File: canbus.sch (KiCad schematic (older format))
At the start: 12 parts

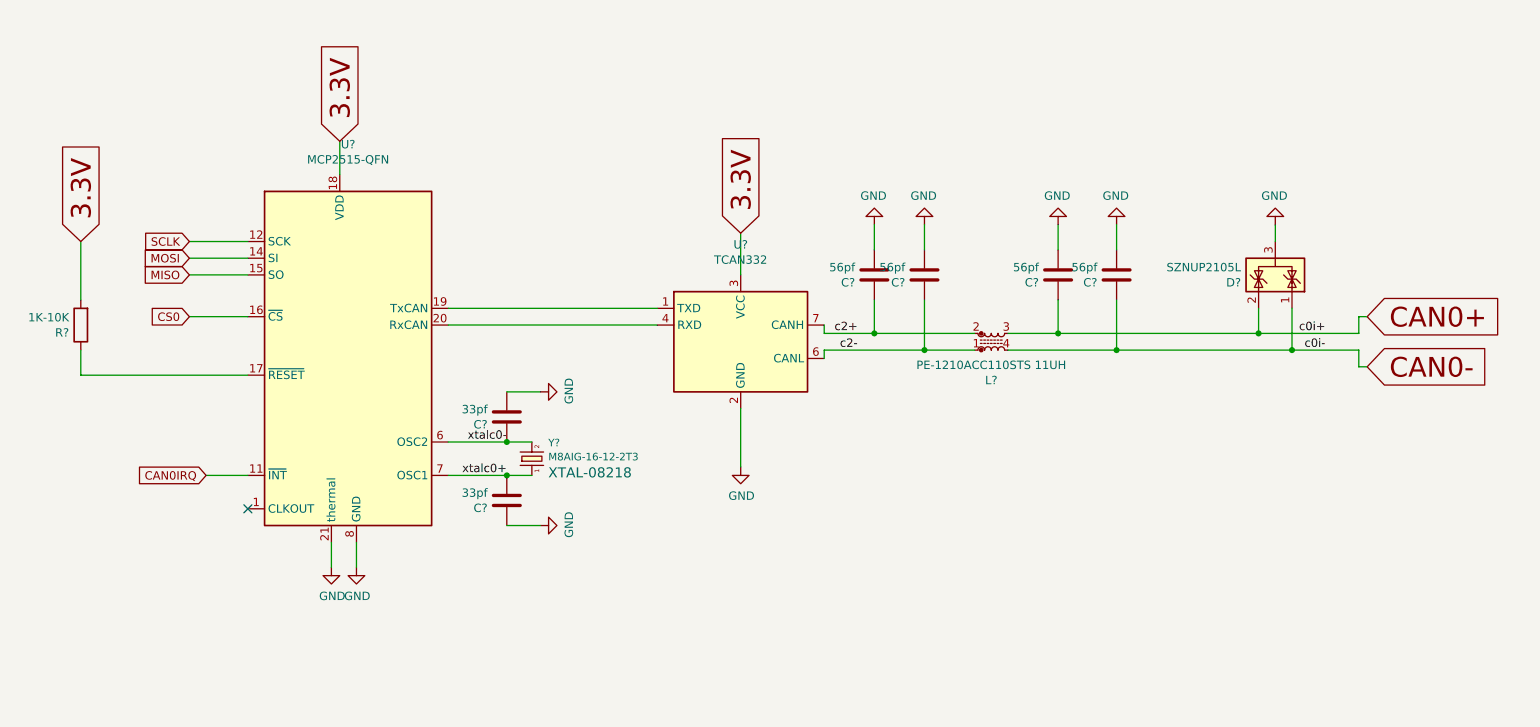
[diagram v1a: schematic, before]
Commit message: Esp32 & Canbus Sch. edited.
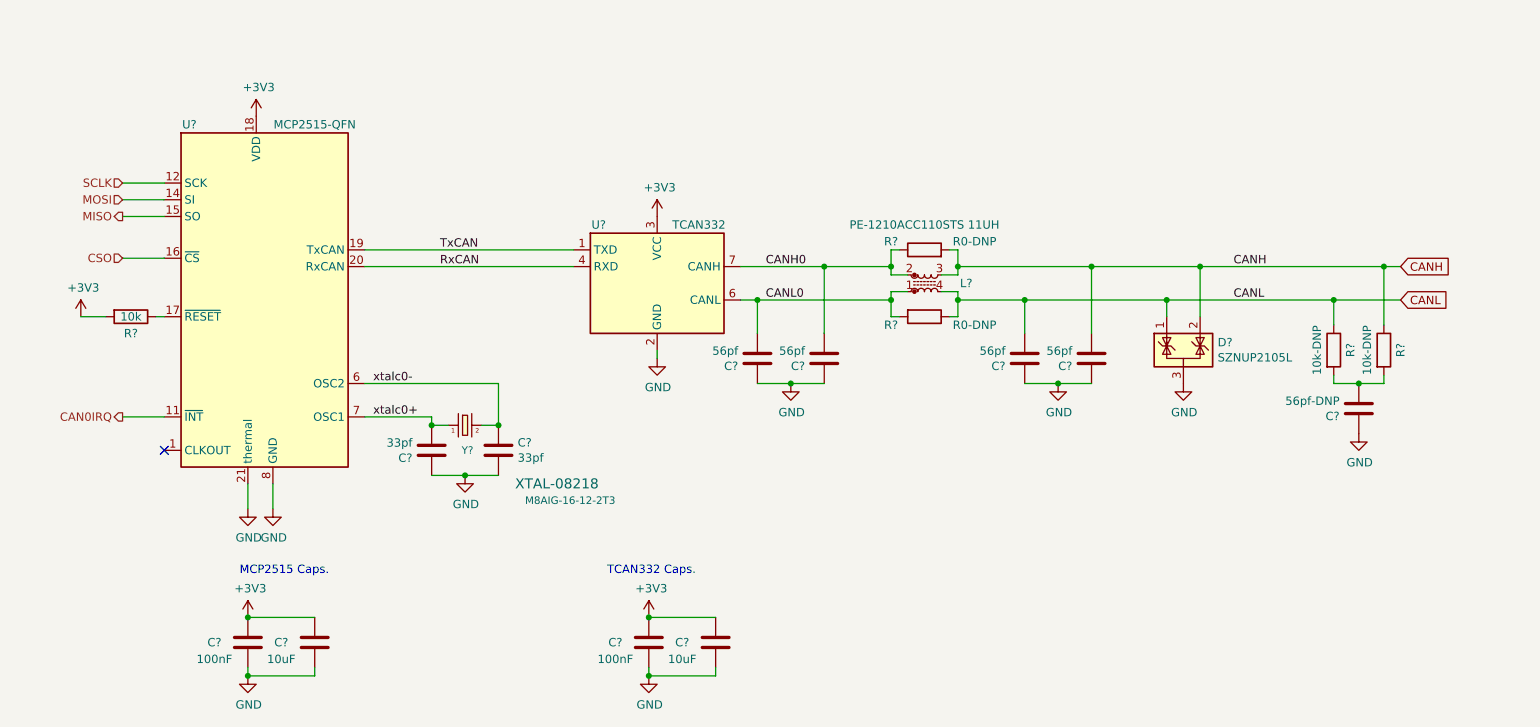
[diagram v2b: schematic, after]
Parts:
- removed C? (x2): 56pf, Capacitor_SMD:C_0603_1608Metric, symbol Device:C
- removed R?: 1K-10K, Resistor_SMD:R_0603_1608Metric, symbol Device:R
- added C? (x2): 10uF, Capacitor_SMD:C_0603_1608Metric, symbol Device:C
- added C? (x2): 100nF, Capacitor_SMD:C_0603_1608Metric, symbol Device:C
- added C? (x2): 56pf, Capacitor_SMD:C_0603_1608Metric, symbol Device:C
- added C?: 56pf-DNP, Capacitor_SMD:C_0603_1608Metric, symbol Device:C
- added R?: 10k, Resistors:0603, symbol Device:R
- added R? (x2): 10k-DNP, Resistors:0603, symbol Device:R
- added R? (x2): R0-DNP, Resistors:0603, symbol Device:R
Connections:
- net GND: now also C?.1, C?.1, C?.1, C?.1, C?.1, C?.2, C?.2, C?.2, C?.2; no longer C?.2, C?.2
- net at U?.17 (~RESET): now also R?.1
- net TxCAN: now reaches U?.1 (TXD), U?.19 (TxCAN)
- net RxCAN: now reaches U?.20 (RxCAN), U?.4 (RXD)
- net 3.3V renamed +3V3
- net +3V3: now also C?.1, C?.1, C?.1, C?.1, R?.2
- net CAN0+ renamed CANH
- net CANH: now also C?.2, R?.1, R?.2
- net CAN0- renamed CANL
- net CANL: now also C?.2, R?.1, R?.1
- net CS0 renamed CSO
- net c2+ renamed CANH0
- net CANH0: now also C?.2, R?.1; no longer C?.1
- net c2- renamed CANL0
- net CANL0: now also C?.2, R?.2; no longer C?.1
- new net: C?.2, R?.2, R?.2
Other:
- note added: "MCP2515 Caps."
- note added: "TCAN332 Caps."
- moved on the sheet: C?, D?, L?, U?, Y?

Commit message: Power Sch. Updated.
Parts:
- gave numbers to parts that had none: 21

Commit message: Power section placement completed.
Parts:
- R17: renamed from R13; footprint Resistors:0603 -> Resistor_SMD:R_0603_1608Metric
- R18: renamed from R14; footprint Resistors:0603 -> Resistor_SMD:R_0603_1608Metric
- R19: renamed from R15; footprint Resistors:0603 -> Resistor_SMD:R_0603_1608Metric
- R20: renamed from R16; footprint Resistors:0603 -> Resistor_SMD:R_0603_1608Metric
- R21: renamed from R17; footprint Resistors:0603 -> Resistor_SMD:R_0603_1608Metric
- renumbered C25 to C29, C26 to C30, C27 to C31, C28 to C32, C29 to C33, C30 to C34, C31 to C35, C32 to C36, C33 to C37, C34 to C38, C35 to C39

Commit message: PCB design updated.
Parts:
- C39: value 56pf-DNP -> 4.7nf-DNP
- R20, R21: value 10k-DNP -> 60R-DNP
- Y1: symbol SparkFun-Clocks:CRYSTAL-16MHZSMD-5X3.2 -> OLIMEX_Devices:Crystal_4P
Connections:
- net GND: now also Y1.2, Y1.4
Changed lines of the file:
@@
 L power:GND #PWR053
 U 1 1 603F92B2
-P 4200 4550
-F 0 "#PWR053" H 4200 4300 50  0001 C CNN
-F 1 "GND" H 4205 4377 50  0000 C CNN
-F 2 "" H 4200 4550 50  0001 C CNN
-F 3 "" H 4200 4550 50  0001 C CNN
-	1    4200 4550
+P 4250 4550
+F 0 "#PWR053" H 4250 4300 50  0001 C CNN
+F 1 "GND" H 4255 4377 50  0000 C CNN
+F 2 "" H 4250 4550 50  0001 C CNN
+F 3 "" H 4250 4550 50  0001 C CNN
+	1    4250 4550
 	1    0    0    -1
 $EndComp
@@
 $EndComp
 $Comp
-L SparkFun-Clocks:CRYSTAL-16MHZSMD-5X3.2 Y1
+L OLIMEX_Devices:Crystal_4P Y1
 U 1 1 603F9360
 P 4200 4250
-F 0 "Y1" H 4250 4100 45  0000 R CNN
+F 0 "Y1" H 4250 4350 45  0000 R CNN
 F 1 "M8AIG-16-12-2T3" H 5100 3800 45  0000 R CNN
 F 2 "Crystal:Crystal_SMD_Abracon_ABM8G-4Pin_3.2x2.5mm" H 4200 4450 20  0001 C CNN
@@
 Wire Wire Line
 	2150 3000 2400 3000
-Wire Wire Line
-	4000 4550 4200 4550
-Connection ~ 4200 4550
-Wire Wire Line
-	4200 4550 4400 4550
 Wire Wire Line
 	4000 4250 4100 4250
@@
 AR Path="/603BB897/6056AFC6" Ref="R20"  Part="1"
 F 0 "R20" V 9500 3800 50  0000 C CNN
-F 1 "10k-DNP" V 9300 3800 50  0000 C CNN
+F 1 "60R-DNP" V 9300 3800 50  0000 C CNN
 F 2 "Resistor_SMD:R_0603_1608Metric" V 9330 3800 50  0001 C CNN
 F 3 "~" H 9400 3800 50  0001 C CNN
@@
 AR Path="/603BB897/6056BD24" Ref="R21"  Part="1"
 F 0 "R21" V 9800 3800 50  0000 C CNN
-F 1 "10k-DNP" V 9600 3800 50  0000 C CNN
+F 1 "60R-DNP" V 9600 3800 50  0000 C CNN
 F 2 "Resistor_SMD:R_0603_1608Metric" V 9630 3800 50  0001 C CNN
 F 3 "~" H 9700 3800 50  0001 C CNN
@@
 P 9550 4150
 F 0 "C39" H 9665 4196 50  0000 L CNN
-F 1 "56pf-DNP" H 9665 4105 50  0000 L CNN
+F 1 "4.7nf-DNP" H 9665 4105 50  0000 L CNN
 F 2 "Capacitor_SMD:C_0603_1608Metric" H 9588 4000 50  0001 C CNN
 F 3 "~" H 9550 4150 50  0001 C CNN
@@
 Text Label 8800 3500 0    50   ~ 0
 CANL
+Connection ~ 4250 4550
+Wire Wire Line
+	4250 4550 4400 4550
+Wire Wire Line
+	4000 4550 4250 4550
+Wire Wire Line
+	4150 4350 4150 4400
+Wire Wire Line
+	4150 4400 4250 4400
+Wire Wire Line
+	4250 4400 4250 4350
+Wire Wire Line
+	4250 4400 4250 4550
+Connection ~ 4250 4400
 $EndSCHEMATC
